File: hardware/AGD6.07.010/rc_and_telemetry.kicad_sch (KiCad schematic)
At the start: 0 parts

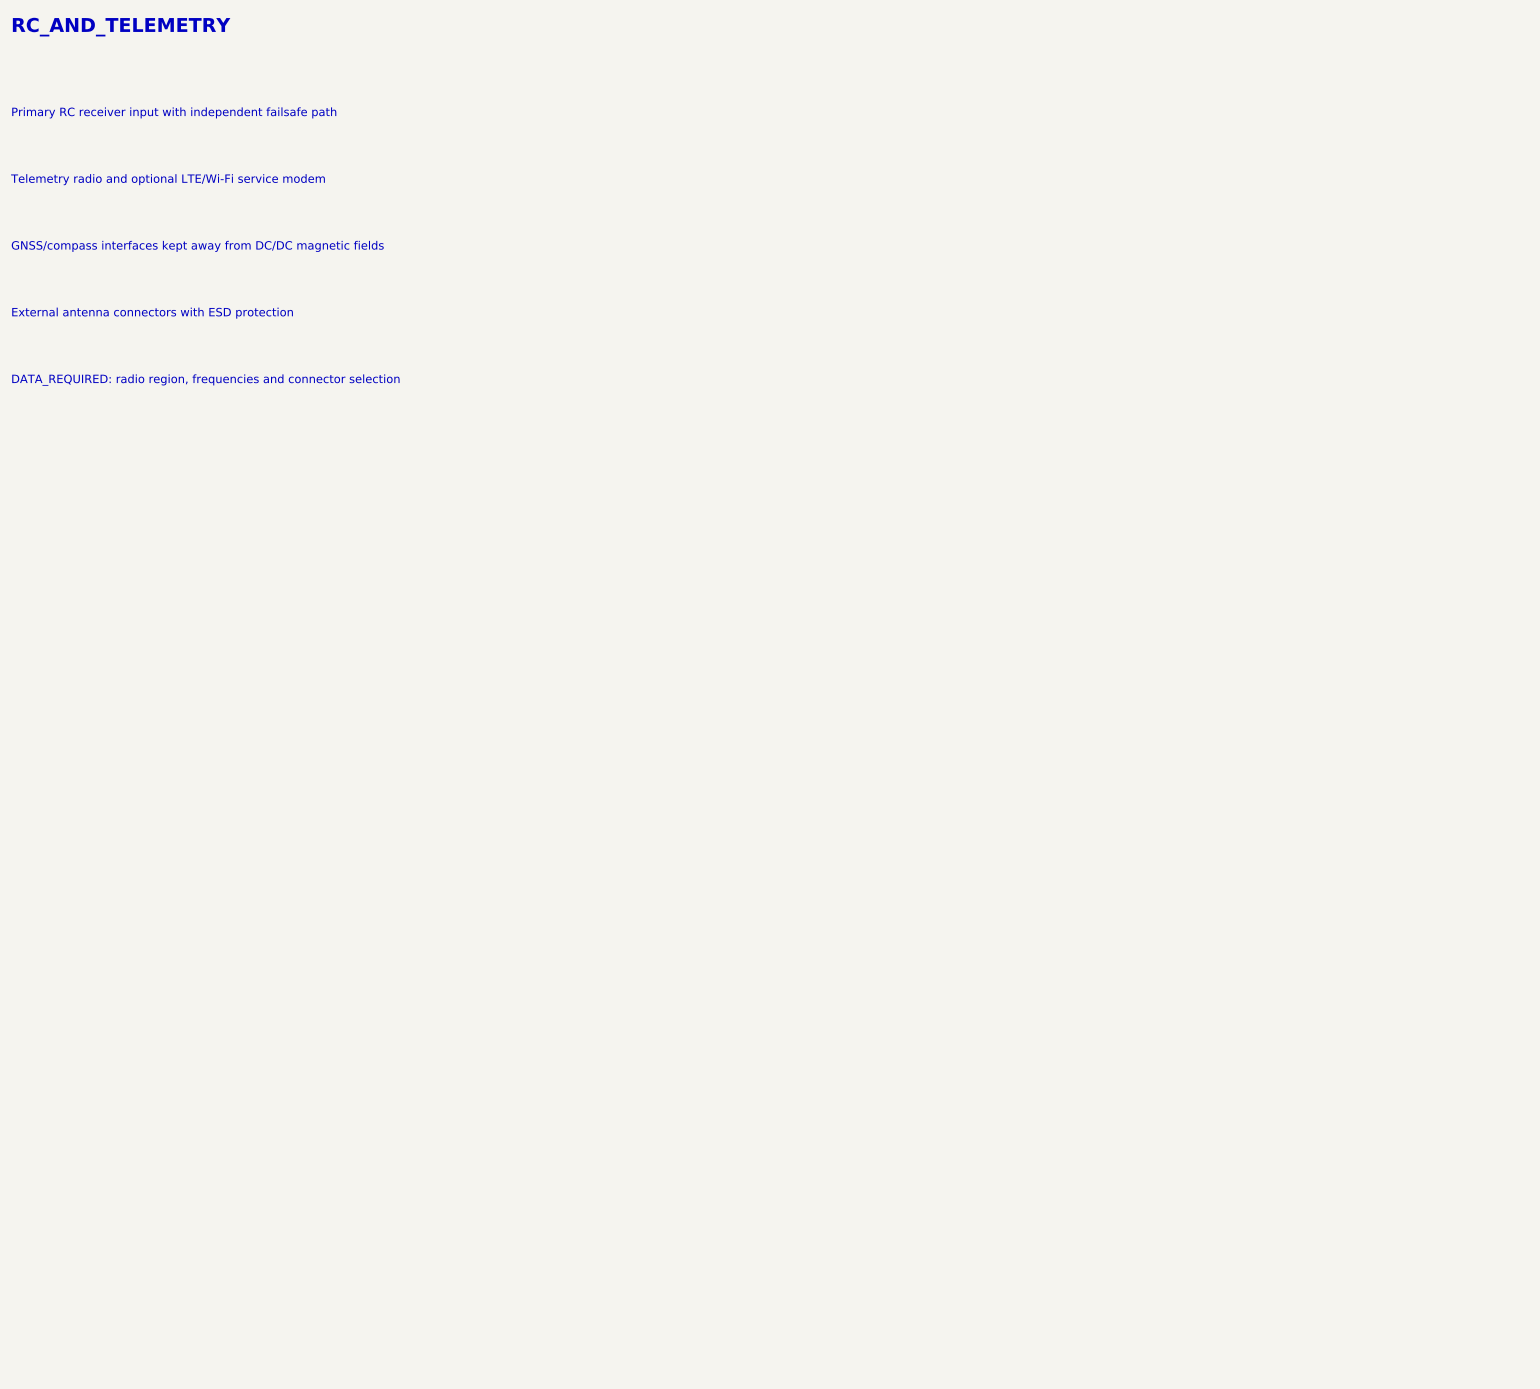
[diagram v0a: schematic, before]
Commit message: Draw full AGD6.07.010 schematic per integrated_avionics_board spec
All ten sheets now carry components: 14S input with hot-swap and power
monitor, 12/5/3.3 V rails and a separate 12 V AI channel with soft-start
and current telemetry, Pixhawk connectors, CAN1/CAN2 hub with chokes,
ESD and switchable termination, sensor conditioning, SIYI and radar,
AI interface and watchdog, protected 12 V switches with diagnostics,
fan/heater control, cameras and Ethernet. Open choices are recorded in
DECISIONS.md; datasheet-dependent values are flagged CHECK_DATASHEET.

ERC: no errors. All 752 intended pin connections match the KiCad netlist.

Co-Authored-By: Claude Opus 5.5 <noreply@anthropic.com>
Claude-Session: https://claude.ai/code/session_01Qk7uTKdi6YbndB9fGuguYV
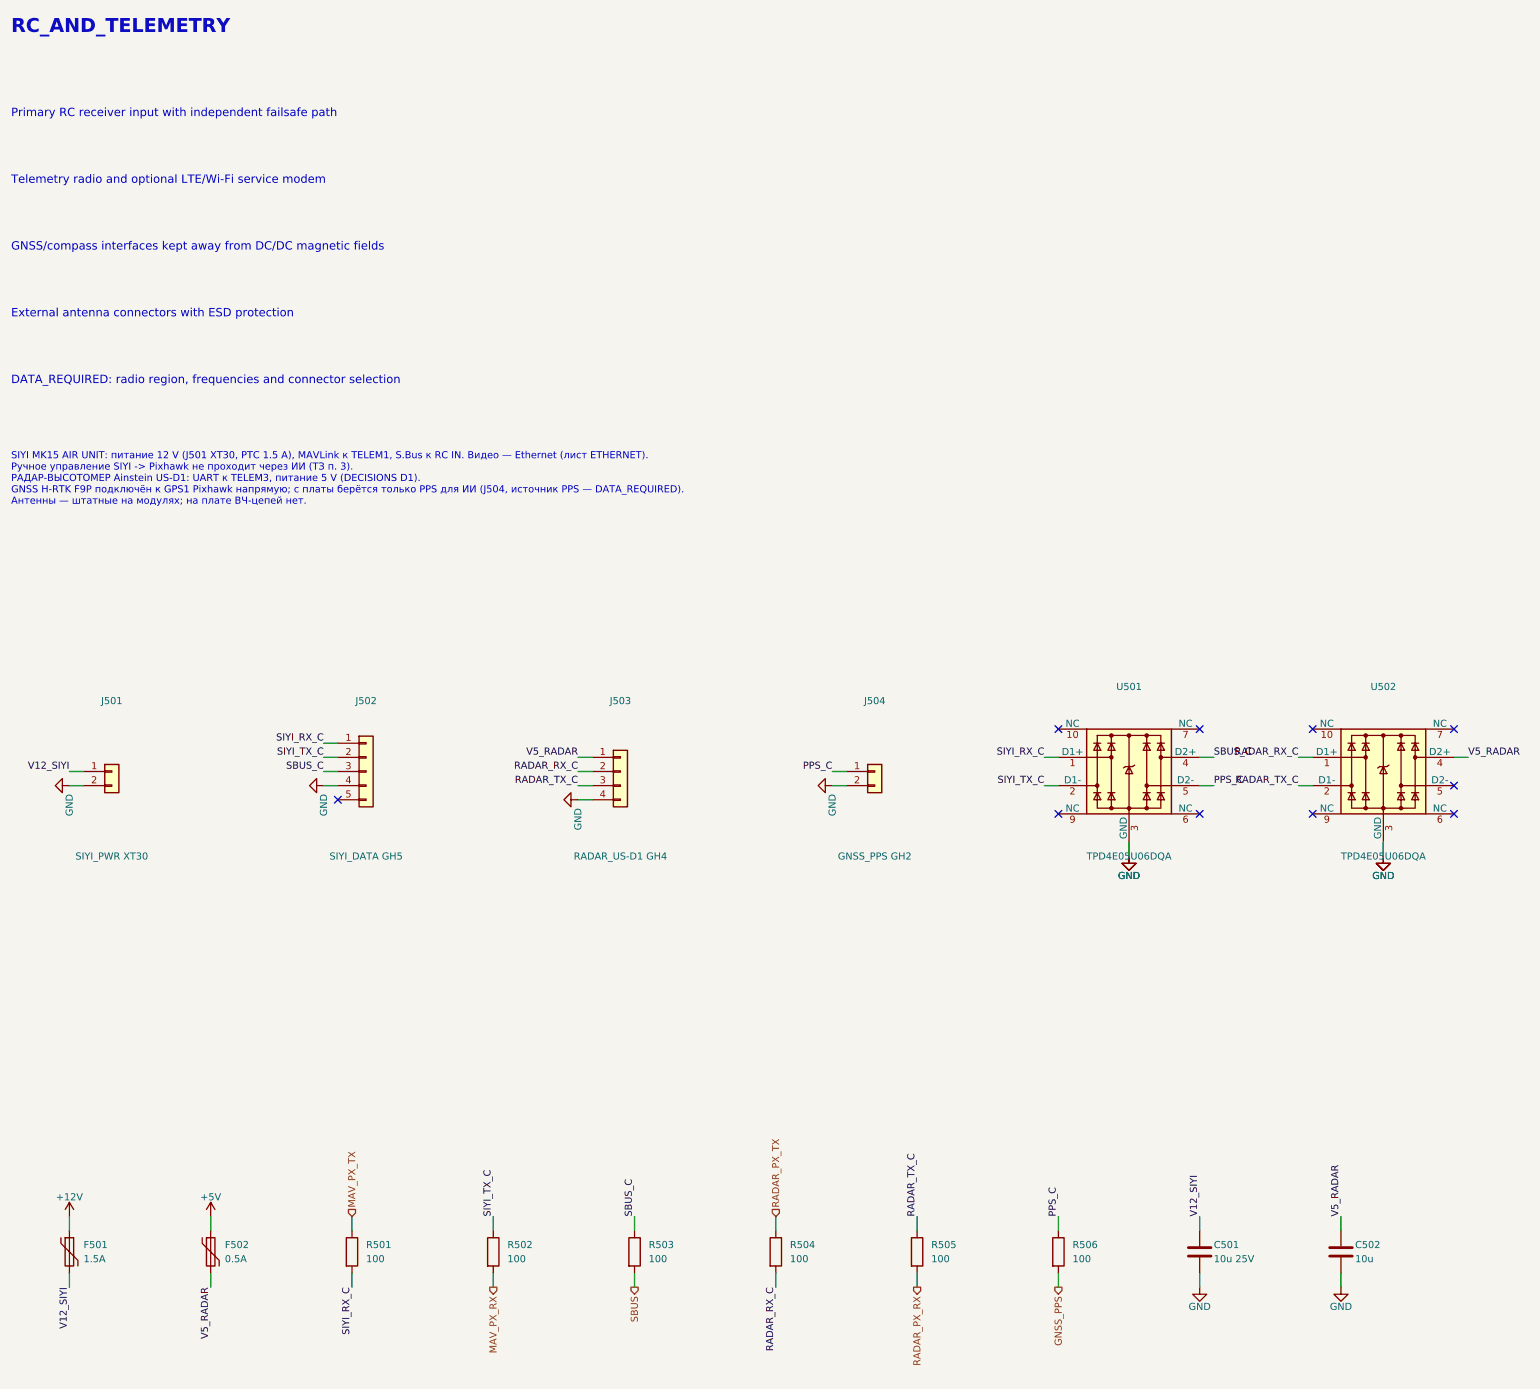
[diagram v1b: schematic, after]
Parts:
- added C501: 10u 25V, Capacitor_SMD:C_1210_3225Metric, symbol Device:C
- added C502: 10u, Capacitor_SMD:C_0805_2012Metric, symbol Device:C
- added F501: 1.5A, Fuse:Fuse_1812_4532Metric, symbol Device:Polyfuse
- added F502: 0.5A, Fuse:Fuse_1206_3216Metric, symbol Device:Polyfuse
- added J501: SIYI_PWR XT30, Connector_AMASS:AMASS_XT30PW-F_1x02_P2.50mm_Horizontal, symbol Connector_Generic:Conn_01x02
- added J502: SIYI_DATA GH5, Connector_JST:JST_GH_SM05B-GHS-TB_1x05-1MP_P1.25mm_Horizontal, symbol Connector_Generic:Conn_01x05
- added J503: RADAR_US-D1 GH4, Connector_JST:JST_GH_SM04B-GHS-TB_1x04-1MP_P1.25mm_Horizontal, symbol Connector_Generic:Conn_01x04
- added J504: GNSS_PPS GH2, Connector_JST:JST_GH_SM02B-GHS-TB_1x02-1MP_P1.25mm_Horizontal, symbol Connector_Generic:Conn_01x02
- added R501, R502, R503, R504, R505, R506: 100, Resistor_SMD:R_0402_1005Metric, symbol Device:R
- added U501, U502: TPD4E05U06DQA, Package_SON:USON-10_2.5x1.0mm_P0.5mm, symbol Power_Protection:TPD4E05U06DQA
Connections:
- new net +12V: F501.1
- new net +5V: F502.1
- new net GND: C501.2, C502.2, J501.2 (Pin_2), J502.4 (Pin_4), J503.4 (Pin_4), J504.2 (Pin_2), U501.3 (GND), U501.8 (GND), U502.3 (GND), U502.8 (GND)
- new net GNSS_PPS: R506.2
- new net MAV_PX_RX: R502.2
- new net MAV_PX_TX: R501.1
- new net PPS_C: J504.1 (Pin_1), R506.1, U501.5 (D2-)
- new net RADAR_PX_RX: R505.2
- new net RADAR_PX_TX: R504.1
- new net RADAR_RX_C: J503.2 (Pin_2), R504.2, U502.1 (D1+)
- new net RADAR_TX_C: J503.3 (Pin_3), R505.1, U502.2 (D1-)
- new net SBUS: R503.2
- new net SBUS_C: J502.3 (Pin_3), R503.1, U501.4 (D2+)
- new net SIYI_RX_C: J502.1 (Pin_1), R501.2, U501.1 (D1+)
- new net SIYI_TX_C: J502.2 (Pin_2), R502.1, U501.2 (D1-)
- new net V12_SIYI: C501.1, F501.2, J501.1 (Pin_1)
- new net V5_RADAR: C502.1, F502.2, J503.1 (Pin_1), U502.4 (D2+)
- no-connect marks 0 -> 10
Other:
- note added: "SIYI MK15 AIR UNIT: питание 12 V (J501 XT30, PTC 1.5 A), MAVLink к TELEM1, S.Bus к RC IN. Видео — Ethernet (лист ETHERNET). Ручное управление SIYI -> Pixhawk не проходит через ИИ (ТЗ п. 3). РАДАР-ВЫСОТОМЕР Ainstein US-D1: UART к TELEM3, питание 5 V (DECISIONS D1). GNSS H-RTK F9P подключён к GPS1 Pixhawk напрямую; с платы берётся только PPS для ИИ (J504, источник PPS — DATA_REQUIRED). Антенны — шт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"
- company: (none) -> АГД6.07.010
- title: (none) -> RC_AND_TELEMETRY
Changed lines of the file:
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@@
-(kicad_sch
-	(version 20260306)
-	(generator "eeschema")
-	(generator_version "10.0")
-	(paper "A4")
-	(text "DATA_REQUIRED: radio region, frequencies and connector selection"
-		(exclude_from_sim no)
-		(at 20 83 0)
-		(effects
-			(font
-				(size 1.5 1.5)
-			)
-			(justify left bottom)
-		)
-	)
-	(text "Primary RC receiver input with independent failsafe path"
-		(exclude_from_sim no)
-		(at 20 35 0)
-		(effects
-			(font
-				(size 1.5 1.5)
-			)
-			(justify left bottom)
-		)
-	)
-	(text "GNSS/compass interfaces kept away from DC/DC magnetic fields"
-		(exclude_from_sim no)
-		(at 20 59 0)
-		(effects
-			(font
-				(size 1.5 1.5)
-			)
-			(justify left bottom)
-		)
-	)
-	(text "Telemetry radio and optional LTE/Wi-Fi service modem"
-		(exclude_from_sim no)
-		(at 20 47 0)
-		(effects
-			(font
-				(size 1.5 1.5)
-			)
-			(justify left bottom)
-		)
-	)
-	(text "RC_AND_TELEMETRY"
-		(exclude_from_sim no)
-		(at 20 20 0)
-		(effects
-			(font
-				(size 2.5 2.5)
-				(bold yes)
-			)
-			(justify left bottom)
-		)
-	)
-	(text "External antenna connectors with ESD protection"
-		(exclude_from_sim no)
-		(at 20 71 0)
-		(effects
-			(font
-				(size 1.5 1.5)
-			)
-			(justify left bottom)
-		)
-	)
-	(sheet_instances
-		(path "/"
-			(page "1")
-		)
-	)
-)
